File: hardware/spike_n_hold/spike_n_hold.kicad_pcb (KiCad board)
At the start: 2 copper layers, 63 x 110.5 mm, 61 parts, among them J1 input_trigger_2, J2 input_trigger_1, J3 to_solenoid_2, J4 to_solenoid_1, J5 Conn_01x02, J6 Conn_01x02, J7 Conn_01x02, Q1 MJH11021G, Q2 MJH11021G, Q3 MPSA42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

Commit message: Update board and add gerbers
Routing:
- net +12V: track 217.5 -> 212.0 mm

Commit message: Make inductor's footprint unified across system
Now all inductors have the same footprint and component.
Some minor changes in silk layers: added values to resistors and arranged them in a more readable way
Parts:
- C8: value 100nF -> 10nF
- L1: footprint Inductor_THT:L_Radial_D7.5mm_P3.50mm_Fastron_07P -> Inductor_THT:L_Radial_D10.0mm_P5.00mm_Neosid_SD12_style3
- R17: value 47 -> 330
- moved D17 2.50 mm to (134.5, 53.0)
- moved C15 1.58 mm to (114.5, 36.5)
- moved R16 1.50 mm to (120.0, 40.5)
- moved R17 1.50 mm to (129.0, 40.5)
- moved R18 1.50 mm to (124.5, 40.5)
- moved Q9 1.00 mm to (122.5, 36.5)
- moved L1 0.50 mm to (146.0, 38.5)
- moved U3 0.50 mm to (155.5, 53.0)
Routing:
- net Net-(R17-Pad1): track 27.9 -> 29.6 mm
- net Net-(R15-Pad2): track 33.5 -> 34.6 mm
- net +12V: track 212.0 -> 213.0 mm
- net Net-(D17-Pad2): track 18.7 -> 17.9 mm
- net Net-(C7-Pad2): track 44.1 -> 44.8 mm

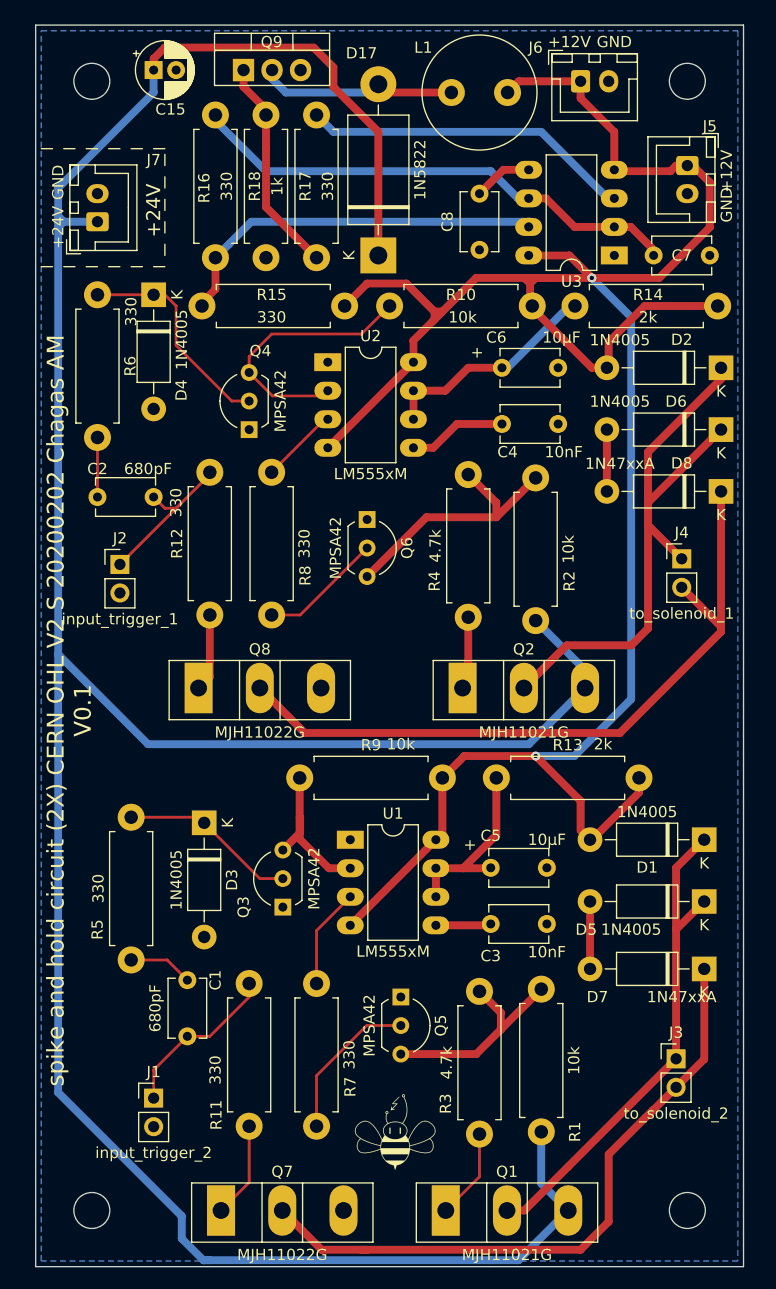
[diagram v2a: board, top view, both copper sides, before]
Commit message: update input pins, so that they are beehive compatible
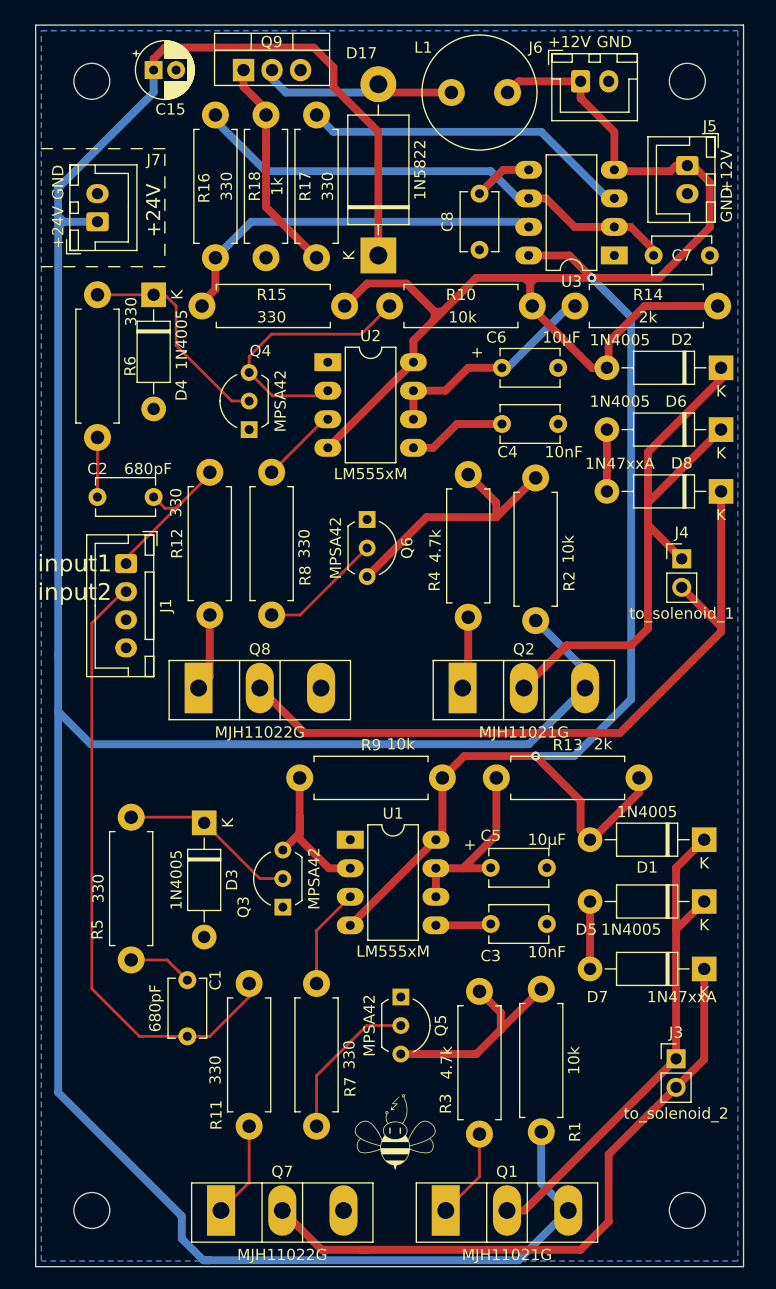
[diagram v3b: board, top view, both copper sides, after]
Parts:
- removed J2: input_trigger_1, Connector_PinHeader_2.54mm:PinHeader_1x02_P2.54mm_Vertical
- J1: value input_trigger_2 -> Conn_01x04_Female; footprint Connector_PinHeader_2.54mm:PinHeader_1x02_P2.54mm_Vertical -> Connector_JST:JST_XH_B4B-XH-A_1x04_P2.50mm_Vertical
- moved J1 47.6 mm to (112.0, 80.4), turned to 270 degrees
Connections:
- J1 pad 1: input_trigger2 -> input_trigger1
- J1 pad 2: GND -> input_trigger2
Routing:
- net input_trigger2: track 14.9 -> 54.5 mm
- net +24V: track 259.2 -> 257.1 mm
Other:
- board text added: "input1"
- board text added: "input2"
- board text added: "spike and hold circuit (2X) CERN OHL V2 S 20200202 Chagas AM & Sobianin I V0.12"
- board text removed: "spike and hold circuit (2X) CERN OHL V2 S 20200202 Chagas AM V0.1"

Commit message: boards review
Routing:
- net +24V: track 257.1 -> 244.8 mm
